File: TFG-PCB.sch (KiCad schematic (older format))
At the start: 141 parts, among them J1 TYPE-C-31-M-12, SW1 SW_Push, U1 ATmega32U4-AU, Y1 16MHz

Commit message: Almost all wiring done
Practically finished wiring
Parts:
- added C8, C9: 1uF, Capacitor_SMD:C_0805_2012Metric, symbol Device:C_Small
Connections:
- net +5V: now also U1.42 (AREF), C8.1, C9.1
- net GND: now also C8.2, C9.2
- no-connect marks 3 -> 2
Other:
- moved on the sheet: C4, C5, C6, C7
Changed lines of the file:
@@
 $EndDescr
-$Comp
-L MCU_Microchip_ATmega:ATmega32U4-AU U1
-U 1 1 60FAC7F6
-P 3500 8500
-F 0 "U1" H 3350 7450 50  0000 C CNN
-F 1 "ATmega32U4-AU" H 3350 7350 50  0000 C CNN
-F 2 "Package_QFP:TQFP-44_10x10mm_P0.8mm" H 3500 8500 50  0001 C CIN
-F 3 "http://ww1.microchip.com/downloads/en/DeviceDoc/Atmel-7766-8-bit-AVR-ATmega16U4-32U4_Datasheet.pdf" H 3500 8500 50  0001 C CNN
-	1    3500 8500
-	1    0    0    -1
-$EndComp
 $Comp
 L power:+5V #PWR02
@@
 L Device:C_Small C4
 U 1 1 60FC2802
-P 1050 9400
-F 0 "C4" H 1142 9446 50  0000 L CNN
-F 1 "0.1uF" H 1142 9355 50  0000 L CNN
-F 2 "Capacitor_SMD:C_0805_2012Metric" H 1050 9400 50  0001 C CNN
-F 3 "~" H 1050 9400 50  0001 C CNN
-	1    1050 9400
+P 700 9500
+F 0 "C4" H 792 9546 50  0000 L CNN
+F 1 "0.1uF" H 792 9455 50  0000 L CNN
+F 2 "Capacitor_SMD:C_0805_2012Metric" H 700 9500 50  0001 C CNN
+F 3 "~" H 700 9500 50  0001 C CNN
+	1    700  9500
 	1    0    0    -1
 $EndComp
@@
 L Device:C_Small C5
 U 1 1 60FC2F64
-P 1450 9400
-F 0 "C5" H 1542 9446 50  0000 L CNN
-F 1 "0.1uF" H 1542 9355 50  0000 L CNN
-F 2 "Capacitor_SMD:C_0805_2012Metric" H 1450 9400 50  0001 C CNN
-F 3 "~" H 1450 9400 50  0001 C CNN
-	1    1450 9400
+P 1100 9500
+F 0 "C5" H 1192 9546 50  0000 L CNN
+F 1 "0.1uF" H 1192 9455 50  0000 L CNN
+F 2 "Capacitor_SMD:C_0805_2012Metric" H 1100 9500 50  0001 C CNN
+F 3 "~" H 1100 9500 50  0001 C CNN
+	1    1100 9500
 	1    0    0    -1
 $EndComp
@@
 L Device:C_Small C6
 U 1 1 60FC3F36
-P 1850 9400
-F 0 "C6" H 1942 9446 50  0000 L CNN
-F 1 "0.1uF" H 1942 9355 50  0000 L CNN
-F 2 "Capacitor_SMD:C_0805_2012Metric" H 1850 9400 50  0001 C CNN
-F 3 "~" H 1850 9400 50  0001 C CNN
-	1    1850 9400
+P 1500 9500
+F 0 "C6" H 1592 9546 50  0000 L CNN
+F 1 "0.1uF" H 1592 9455 50  0000 L CNN
+F 2 "Capacitor_SMD:C_0805_2012Metric" H 1500 9500 50  0001 C CNN
+F 3 "~" H 1500 9500 50  0001 C CNN
+	1    1500 9500
 	1    0    0    -1
 $EndComp
@@
 L Device:C_Small C7
 U 1 1 60FC41F6
-P 2250 9400
-F 0 "C7" H 2342 9446 50  0000 L CNN
-F 1 "10uF" H 2342 9355 50  0000 L CNN
-F 2 "Capacitor_SMD:C_0805_2012Metric" H 2250 9400 50  0001 C CNN
-F 3 "~" H 2250 9400 50  0001 C CNN
-	1    2250 9400
-	1    0    0    -1
-$EndComp
-Wire Wire Line
-	1050 9500 1450 9500
-Wire Wire Line
-	1450 9500 1650 9500
-Connection ~ 1450 9500
-Wire Wire Line
-	1850 9500 2250 9500
-Connection ~ 1850 9500
-Wire Wire Line
-	1050 9300 1450 9300
-Wire Wire Line
-	1450 9300 1650 9300
-Connection ~ 1450 9300
-Wire Wire Line
-	1850 9300 2250 9300
-Connection ~ 1850 9300
+P 1900 9500
+F 0 "C7" H 1992 9546 50  0000 L CNN
+F 1 "10uF" H 1992 9455 50  0000 L CNN
+F 2 "Capacitor_SMD:C_0805_2012Metric" H 1900 9500 50  0001 C CNN
+F 3 "~" H 1900 9500 50  0001 C CNN
+	1    1900 9500
+	1    0    0    -1
+$EndComp
+Wire Wire Line
+	700  9600 1100 9600
+Connection ~ 1100 9600
+Wire Wire Line
+	1500 9600 1700 9600
+Connection ~ 1500 9600
+Wire Wire Line
+	700  9400 1100 9400
+Connection ~ 1100 9400
+Wire Wire Line
+	1500 9400 1700 9400
+Connection ~ 1500 9400
 $Comp
 L power:+5V #PWR012
 U 1 1 60FC5E59
-P 1650 9150
-F 0 "#PWR012" H 1650 9000 50  0001 C CNN
-F 1 "+5V" H 1665 9323 50  0000 C CNN
-F 2 "" H 1650 9150 50  0001 C CNN
-F 3 "" H 1650 9150 50  0001 C CNN
-	1    1650 9150
+P 1700 9250
+F 0 "#PWR012" H 1700 9100 50  0001 C CNN
+F 1 "+5V" H 1715 9423 50  0000 C CNN
+F 2 "" H 1700 9250 50  0001 C CNN
+F 3 "" H 1700 9250 50  0001 C CNN
+	1    1700 9250
 	1    0    0    -1
 $EndComp
@@
 L power:GND #PWR013
 U 1 1 60FC6520
-P 1650 9650
-F 0 "#PWR013" H 1650 9400 50  0001 C CNN
-F 1 "GND" H 1655 9477 50  0000 C CNN
-F 2 "" H 1650 9650 50  0001 C CNN
-F 3 "" H 1650 9650 50  0001 C CNN
-	1    1650 9650
-	1    0    0    -1
-$EndComp
-Wire Wire Line
-	1650 9500 1650 9650
-Connection ~ 1650 9500
-Wire Wire Line
-	1650 9500 1850 9500
-Wire Wire Line
-	1650 9300 1650 9150
-Connection ~ 1650 9300
-Wire Wire Line
-	1650 9300 1850 9300
+P 1700 9750
+F 0 "#PWR013" H 1700 9500 50  0001 C CNN
+F 1 "GND" H 1705 9577 50  0000 C CNN
+F 2 "" H 1700 9750 50  0001 C CNN
+F 3 "" H 1700 9750 50  0001 C CNN
+	1    1700 9750
+	1    0    0    -1
+$EndComp
+Wire Wire Line
+	1700 9600 1700 9750
+Wire Wire Line
+	1700 9400 1700 9250
 $Comp
 L power:+5V #PWR05
@@
 Text Label 2650 8100 0    50   ~ 0
 D_N
-NoConn ~ 2900 7600
+$Comp
+L MCU_Microchip_ATmega:ATmega32U4-AU U1
+U 1 1 60FAC7F6
+P 3500 8500
+F 0 "U1" H 3350 7450 50  0000 C CNN
+F 1 "ATmega32U4-AU" H 3350 7350 50  0000 C CNN
+F 2 "Package_QFP:TQFP-44_10x10mm_P0.8mm" H 3500 8500 50  0001 C CIN
+F 3 "http://ww1.microchip.com/downloads/en/DeviceDoc/Atmel-7766-8-bit-AVR-ATmega16U4-32U4_Datasheet.pdf" H 3500 8500 50  0001 C CNN
+	1    3500 8500
+	1    0    0    -1
+$EndComp
+Wire Wire Line
+	2900 7600 2800 7600
+$Comp
+L power:+5V #PWR015
+U 1 1 612F94FF
+P 2800 7600
+F 0 "#PWR015" H 2800 7450 50  0001 C CNN
+F 1 "+5V" H 2815 7773 50  0000 C CNN
+F 2 "" H 2800 7600 50  0001 C CNN
+F 3 "" H 2800 7600 50  0001 C CNN
+	1    2800 7600
+	1    0    0    -1
+$EndComp
+$Comp
+L Device:C_Small C8
+U 1 1 612F97A1
+P 2300 9500
+F 0 "C8" H 2392 9546 50  0000 L CNN
+F 1 "1uF" H 2392 9455 50  0000 L CNN
+F 2 "Capacitor_SMD:C_0805_2012Metric" H 2300 9500 50  0001 C CNN
+F 3 "~" H 2300 9500 50  0001 C CNN
+	1    2300 9500
+	1    0    0    -1
+$EndComp
+Wire Wire Line
+	1900 9400 2300 9400
+Connection ~ 1900 9400
+Wire Wire Line
+	1900 9600 2300 9600
+Connection ~ 1900 9600
+Wire Wire Line
+	1100 9600 1500 9600
+Wire Wire Line
+	1100 9400 1500 9400
+$Comp
+L Device:C_Small C9
+U 1 1 6137A440
+P 2650 9500
+F 0 "C9" H 2742 9546 50  0000 L CNN
+F 1 "1uF" H 2742 9455 50  0000 L CNN
+F 2 "Capacitor_SMD:C_0805_2012Metric" H 2650 9500 50  0001 C CNN
+F 3 "~" H 2650 9500 50  0001 C CNN
+	1    2650 9500
+	1    0    0    -1
+$EndComp
+Wire Wire Line
+	2300 9400 2650 9400
+Connection ~ 2300 9400
+Wire Wire Line
+	2300 9600 2650 9600
+Connection ~ 2300 9600
+Connection ~ 1700 9400
+Wire Wire Line
+	1700 9400 1900 9400
+Connection ~ 1700 9600
+Wire Wire Line
+	1700 9600 1900 9600
 $EndSCHEMATC

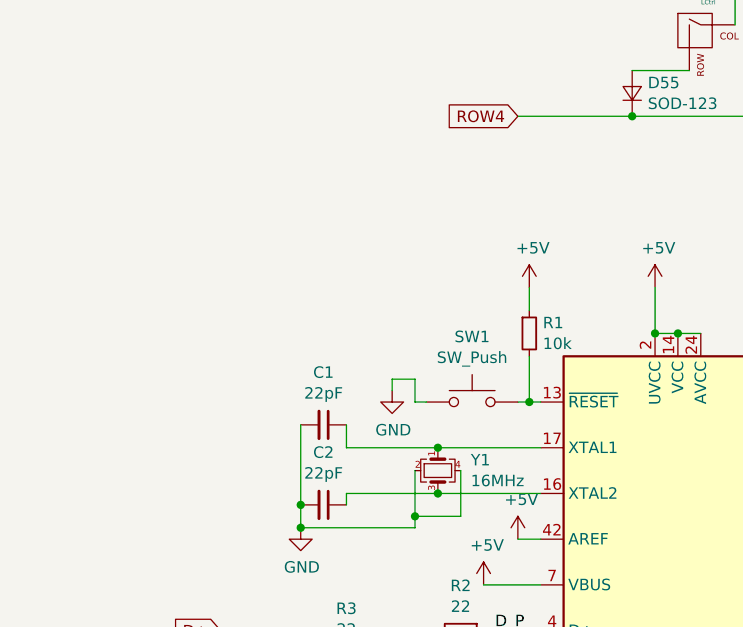
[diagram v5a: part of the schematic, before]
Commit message: Remade Reset button circuit
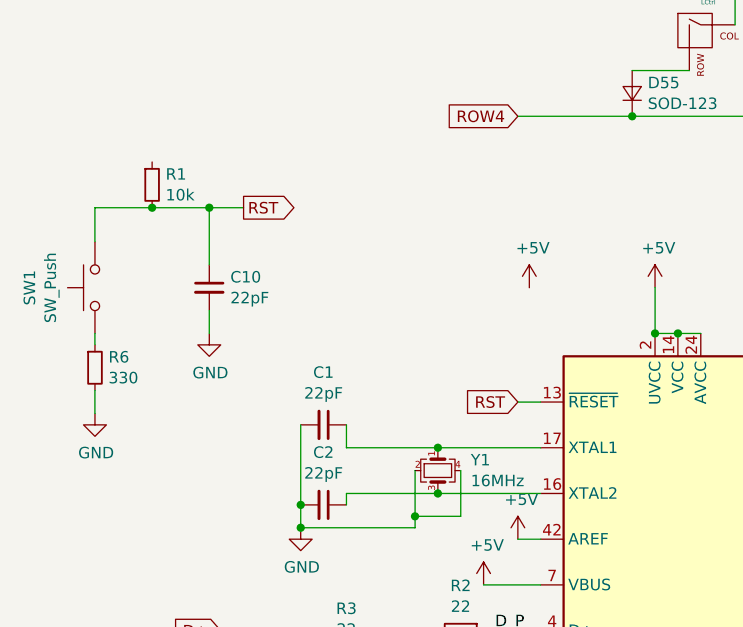
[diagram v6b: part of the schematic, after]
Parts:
- added C10: 22pF, Capacitor_SMD:C_0805_2012Metric, symbol Device:C_Small
- added R6: 330, Resistor_SMD:R_0805_2012Metric, symbol Device:R_Small
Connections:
- net +5V: no longer R1.1
- net GND: now also C10.2, R6.2; no longer SW1.1
- net RST: now reaches R1.2, SW1.2, U1.13 (~RESET)
- net RST: now also C10.1
- new net: R6.1, SW1.1
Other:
- moved on the sheet: R1, SW1
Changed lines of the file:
@@
 L Switch:SW_Push SW1
 U 1 1 60FCFACC
-P 2600 7000
-F 0 "SW1" H 2600 7285 50  0000 C CNN
-F 1 "SW_Push" H 2600 7194 50  0000 C CNN
-F 2 "random-keyboard-parts:SKQG-1155865" H 2600 7200 50  0001 C CNN
-F 3 "~" H 2600 7200 50  0001 C CNN
-	1    2600 7000
-	1    0    0    -1
-$EndComp
-Wire Wire Line
-	2900 7000 2850 7000
-$Comp
-L power:GND #PWR03
-U 1 1 60FD18D7
-P 2250 6950
-F 0 "#PWR03" H 2250 6700 50  0001 C CNN
-F 1 "GND" H 2255 6777 50  0000 C CNN
-F 2 "" H 2250 6950 50  0001 C CNN
-F 3 "" H 2250 6950 50  0001 C CNN
-	1    2250 6950
-	1    0    0    -1
-$EndComp
-Wire Wire Line
-	2400 7000 2350 7000
-Wire Wire Line
-	2350 7000 2350 6900
-Wire Wire Line
-	2350 6900 2250 6900
-Wire Wire Line
-	2250 6900 2250 6950
+P 950 6500
+F 0 "SW1" H 950 6785 50  0000 C CNN
+F 1 "SW_Push" H 950 6694 50  0000 C CNN
+F 2 "random-keyboard-parts:SKQG-1155865" H 950 6700 50  0001 C CNN
+F 3 "~" H 950 6700 50  0001 C CNN
+	1    950  6500
+	0    -1   -1   0
+$EndComp
 $Comp
 L Device:R_Small R1
 U 1 1 60FD30AE
-P 2850 6700
-F 0 "R1" H 2909 6746 50  0000 L CNN
-F 1 "10k" H 2909 6655 50  0000 L CNN
-F 2 "Resistor_SMD:R_0805_2012Metric" H 2850 6700 50  0001 C CNN
-F 3 "~" H 2850 6700 50  0001 C CNN
-	1    2850 6700
-	1    0    0    -1
-$EndComp
-Wire Wire Line
-	2850 7000 2850 6800
-Connection ~ 2850 7000
-Wire Wire Line
-	2850 7000 2800 7000
+P 1200 6050
+F 0 "R1" H 1259 6096 50  0000 L CNN
+F 1 "10k" H 1259 6005 50  0000 L CNN
+F 2 "Resistor_SMD:R_0805_2012Metric" H 1200 6050 50  0001 C CNN
+F 3 "~" H 1200 6050 50  0001 C CNN
+	1    1200 6050
+	1    0    0    -1
+$EndComp
 $Comp
 L power:+5V #PWR01
@@
 	1    0    0    -1
 $EndComp
-Wire Wire Line
-	2850 6500 2850 6600
 Text GLabel 1500 8000 0    50   Input ~ 0
 D+
@@
 Wire Wire Line
 	1700 9600 1900 9600
+$Comp
+L Device:R_Small R6
+U 1 1 612C3257
+P 950 6850
+F 0 "R6" H 1009 6896 50  0000 L CNN
+F 1 "330" H 1009 6805 50  0000 L CNN
+F 2 "Resistor_SMD:R_0805_2012Metric" H 950 6850 50  0001 C CNN
+F 3 "~" H 950 6850 50  0001 C CNN
+	1    950  6850
+	1    0    0    -1
+$EndComp
+Wire Wire Line
+	2800 7000 2900 7000
+Wire Wire Line
+	950  6150 950  6300
+Wire Wire Line
+	950  6150 1200 6150
+$Comp
+L Device:C_Small C10
+U 1 1 612ED224
+P 1450 6500
+F 0 "C10" H 1542 6546 50  0000 L CNN
+F 1 "22pF" H 1542 6455 50  0000 L CNN
+F 2 "Capacitor_SMD:C_0805_2012Metric" H 1450 6500 50  0001 C CNN
+F 3 "~" H 1450 6500 50  0001 C CNN
+	1    1450 6500
+	1    0    0    -1
+$EndComp
+Connection ~ 1200 6150
+Wire Wire Line
+	1450 6150 1450 6400
+Wire Wire Line
+	1200 6150 1450 6150
+Wire Wire Line
+	950  6950 950  7050
+$Comp
+L power:GND #PWR03
+U 1 1 6133D8E8
+P 950 7050
+F 0 "#PWR03" H 950 6800 50  0001 C CNN
+F 1 "GND" H 955 6877 50  0000 C CNN
+F 2 "" H 950 7050 50  0001 C CNN
+F 3 "" H 950 7050 50  0001 C CNN
+	1    950  7050
+	1    0    0    -1
+$EndComp
+Text GLabel 1600 6150 2    50   Output ~ 0
+RST
+Text GLabel 2800 7000 0    50   Input ~ 0
+RST
+Wire Wire Line
+	1450 6150 1600 6150
+Connection ~ 1450 6150
+$Comp
+L power:GND #PWR?
+U 1 1 6137F5CC
+P 1450 6700
+F 0 "#PWR?" H 1450 6450 50  0001 C CNN
+F 1 "GND" H 1455 6527 50  0000 C CNN
+F 2 "" H 1450 6700 50  0001 C CNN
+F 3 "" H 1450 6700 50  0001 C CNN
+	1    1450 6700
+	1    0    0    -1
+$EndComp
+Wire Wire Line
+	1450 6600 1450 6700
+Wire Wire Line
+	950  6700 950  6750
 $EndSCHEMATC

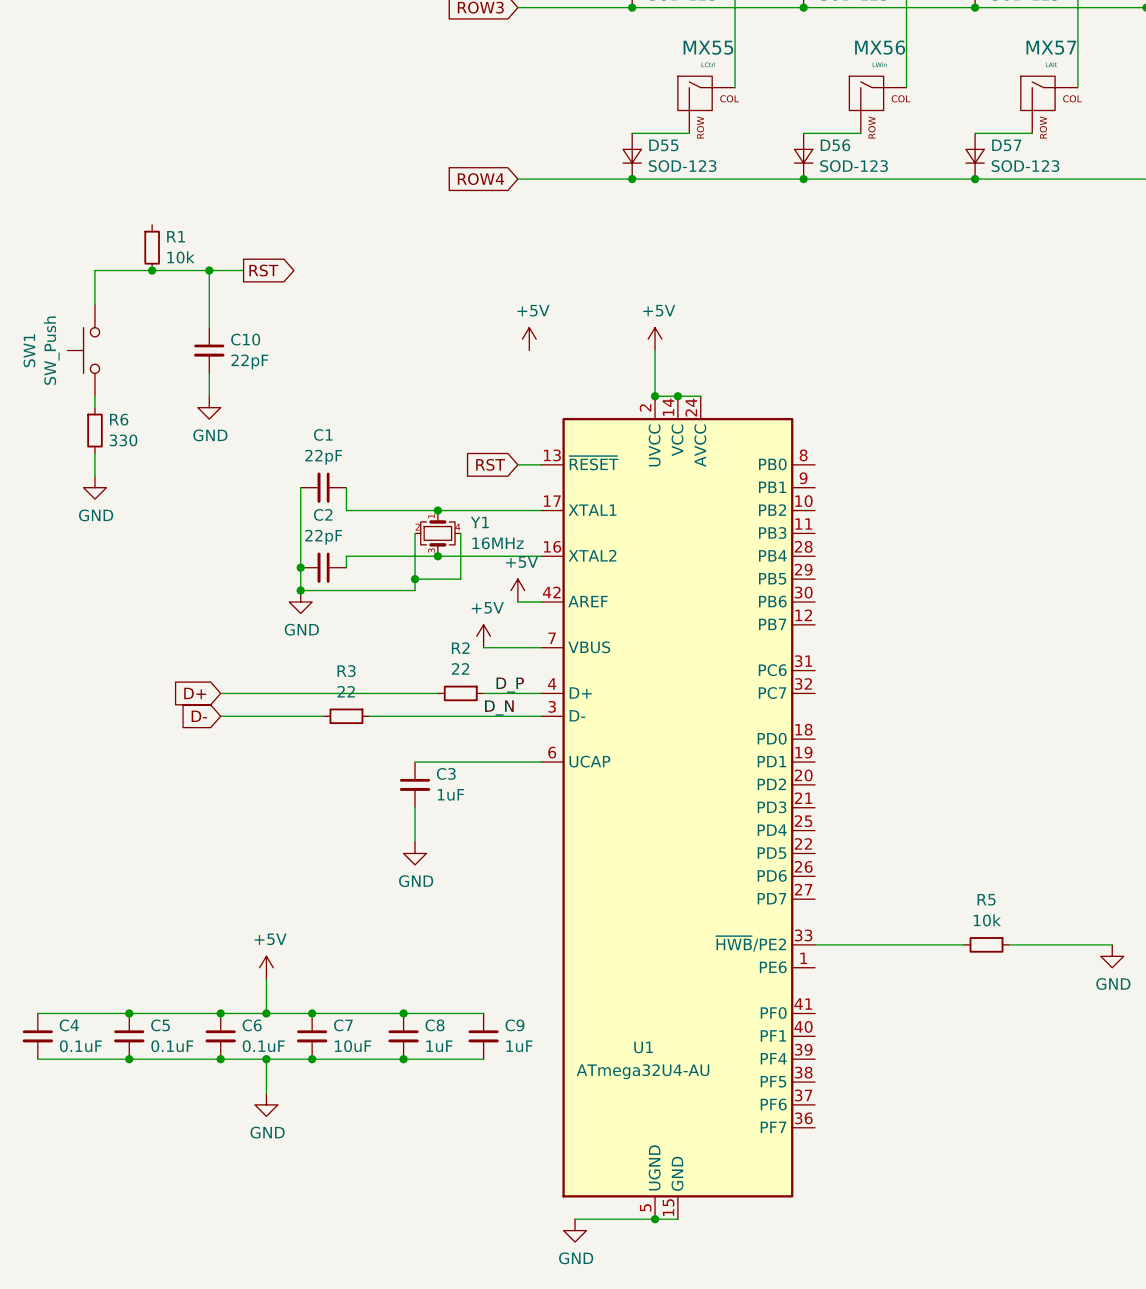
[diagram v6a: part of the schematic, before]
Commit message: PCB finished (almost)
PCB finished aside from ground fill and logo addition
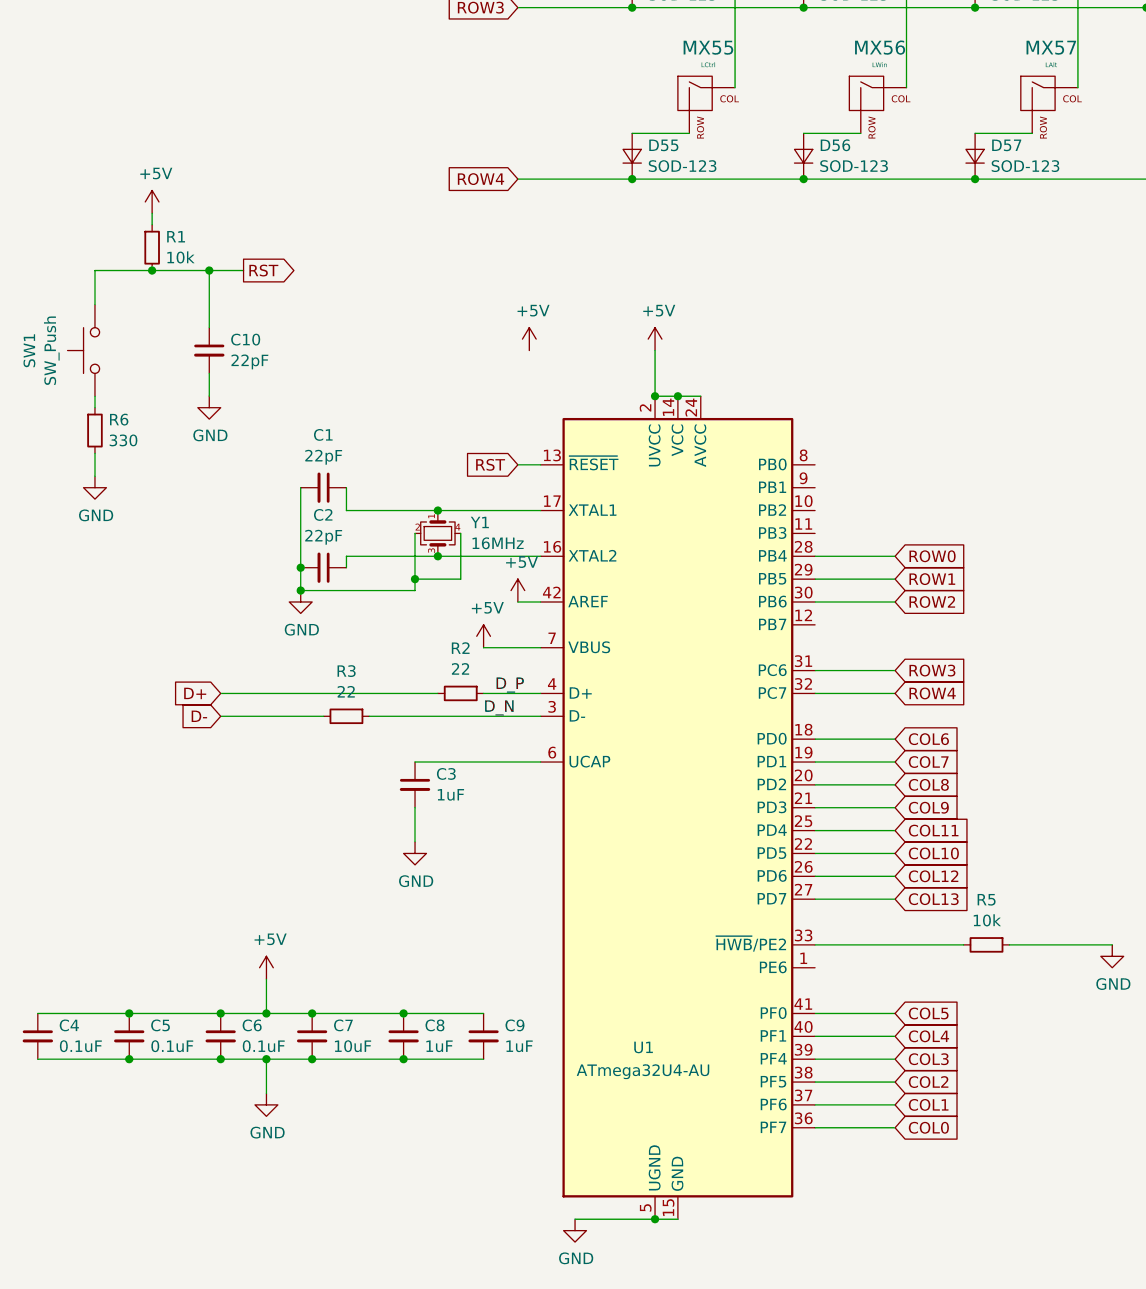
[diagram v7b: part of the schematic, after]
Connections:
- net +5V: now also R1.1
- net COL0: now also U1.36 (PF7)
- net COL1: now also U1.37 (PF6)
- net COL10: now also U1.22 (PD5)
- net COL11: now also U1.25 (PD4)
- net COL12: now also U1.26 (PD6)
- net COL13: now also U1.27 (PD7)
- net COL2: now also U1.38 (PF5)
- net COL3: now also U1.39 (PF4)
- net COL4: now also U1.40 (PF1)
- net COL5: now also U1.41 (PF0)
- net COL6: now also U1.18 (PD0)
- net COL7: now also U1.19 (PD1)
- net COL8: now also U1.20 (PD2)
- net COL9: now also U1.21 (PD3)
- net ROW0: now also U1.28 (PB4)
- net ROW1: now also U1.29 (PB5)
- net ROW2: now also U1.30 (PB6)
- net ROW3: now also U1.31 (PC6)
- net ROW4: now also U1.32 (PC7)
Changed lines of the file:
@@
 Connection ~ 1450 6150
 $Comp
-L power:GND #PWR?
+L power:GND #PWR0101
 U 1 1 6137F5CC
 P 1450 6700
-F 0 "#PWR?" H 1450 6450 50  0001 C CNN
+F 0 "#PWR0101" H 1450 6450 50  0001 C CNN
 F 1 "GND" H 1455 6527 50  0000 C CNN
 F 2 "" H 1450 6700 50  0001 C CNN
@@
 Wire Wire Line
 	950  6700 950  6750
+Wire Wire Line
+	1200 5950 1200 5900
+$Comp
+L power:+5V #PWR?
+U 1 1 613F6851
+P 1200 5900
+F 0 "#PWR?" H 1200 5750 50  0001 C CNN
+F 1 "+5V" H 1215 6073 50  0000 C CNN
+F 2 "" H 1200 5900 50  0001 C CNN
+F 3 "" H 1200 5900 50  0001 C CNN
+	1    1200 5900
+	1    0    0    -1
+$EndComp
+Wire Wire Line
+	4100 9400 4450 9400
+Wire Wire Line
+	4100 9500 4450 9500
+Wire Wire Line
+	4100 9600 4450 9600
+Wire Wire Line
+	4100 9700 4450 9700
+Wire Wire Line
+	4100 9800 4450 9800
+Wire Wire Line
+	4100 9900 4450 9900
+Text GLabel 4450 9900 2    50   Input ~ 0
+COL0
+Text GLabel 4450 9800 2    50   Input ~ 0
+COL1
+Text GLabel 4450 9700 2    50   Input ~ 0
+COL2
+Wire Wire Line
+	4100 8200 4450 8200
+Text GLabel 4450 8200 2    50   Input ~ 0
+COL6
+Text GLabel 4450 8300 2    50   Input ~ 0
+COL7
+Wire Wire Line
+	4100 8300 4450 8300
+Text GLabel 4450 8400 2    50   Input ~ 0
+COL8
+Text GLabel 4450 8500 2    50   Input ~ 0
+COL9
+Text GLabel 4450 8700 2    50   Input ~ 0
+COL10
+Wire Wire Line
+	4100 8400 4450 8400
+Wire Wire Line
+	4100 8500 4450 8500
+Wire Wire Line
+	4100 8700 4450 8700
+Wire Wire Line
+	4100 8600 4450 8600
+Text GLabel 4450 8600 2    50   Input ~ 0
+COL11
+Text GLabel 4450 9600 2    50   Input ~ 0
+COL3
+Text GLabel 4450 9500 2    50   Input ~ 0
+COL4
+Text GLabel 4450 9400 2    50   Input ~ 0
+COL5
+Wire Wire Line
+	4100 8800 4450 8800
+Wire Wire Line
+	4100 8900 4450 8900
+Text GLabel 4450 8800 2    50   Input ~ 0
+COL12
+Text GLabel 4450 8900 2    50   Input ~ 0
+COL13
+Wire Wire Line
+	4100 7500 4450 7500
+Text GLabel 4450 7400 2    50   Input ~ 0
+ROW0
+Wire Wire Line
+	4100 7600 4450 7600
+Text GLabel 4450 7500 2    50   Input ~ 0
+ROW1
+Wire Wire Line
+	4100 7900 4450 7900
+Wire Wire Line
+	4100 8000 4450 8000
+Wire Wire Line
+	4100 7400 4450 7400
+Text GLabel 4450 7600 2    50   Input ~ 0
+ROW2
+Text GLabel 4450 7900 2    50   Input ~ 0
+ROW3
+Text GLabel 4450 8000 2    50   Input ~ 0
+ROW4
 $EndSCHEMATC
